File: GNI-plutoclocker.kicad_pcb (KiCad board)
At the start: 2 copper layers, 49 x 47 mm, 67 parts, among them J1 PLUTO_RF_IN, J2 PLUTO_5V, J3 PLUTO_40MHZ_IN, J4 10MHZ_IN, J5 LNB_OUT, J6 10MHZ_OUT, J7 I2C_PROG, J8 18V_ENA, U1 MIC5504-3.3YM5, U2 MIC5504-1.8YM5, U3 TPS61085, U4 CDCE913

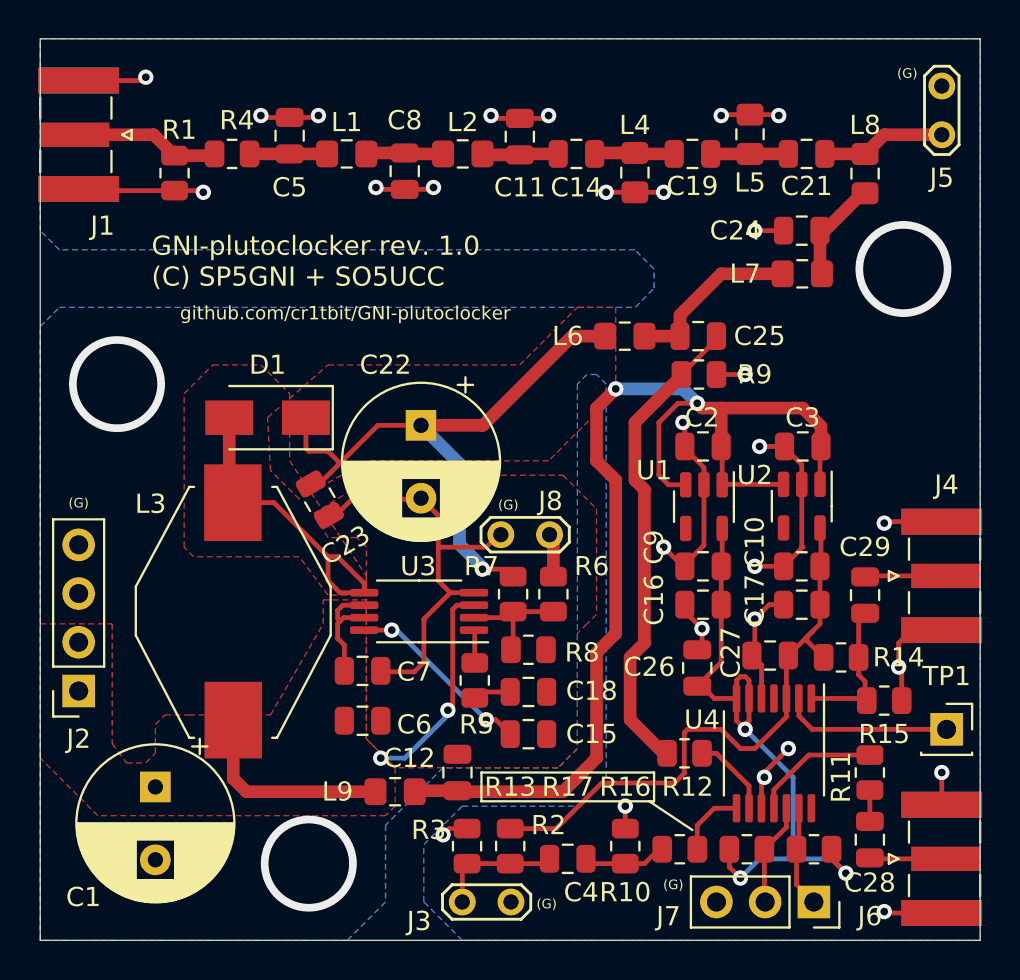
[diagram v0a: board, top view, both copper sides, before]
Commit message: next revision candidate - adding some solderbridge multiplexing options
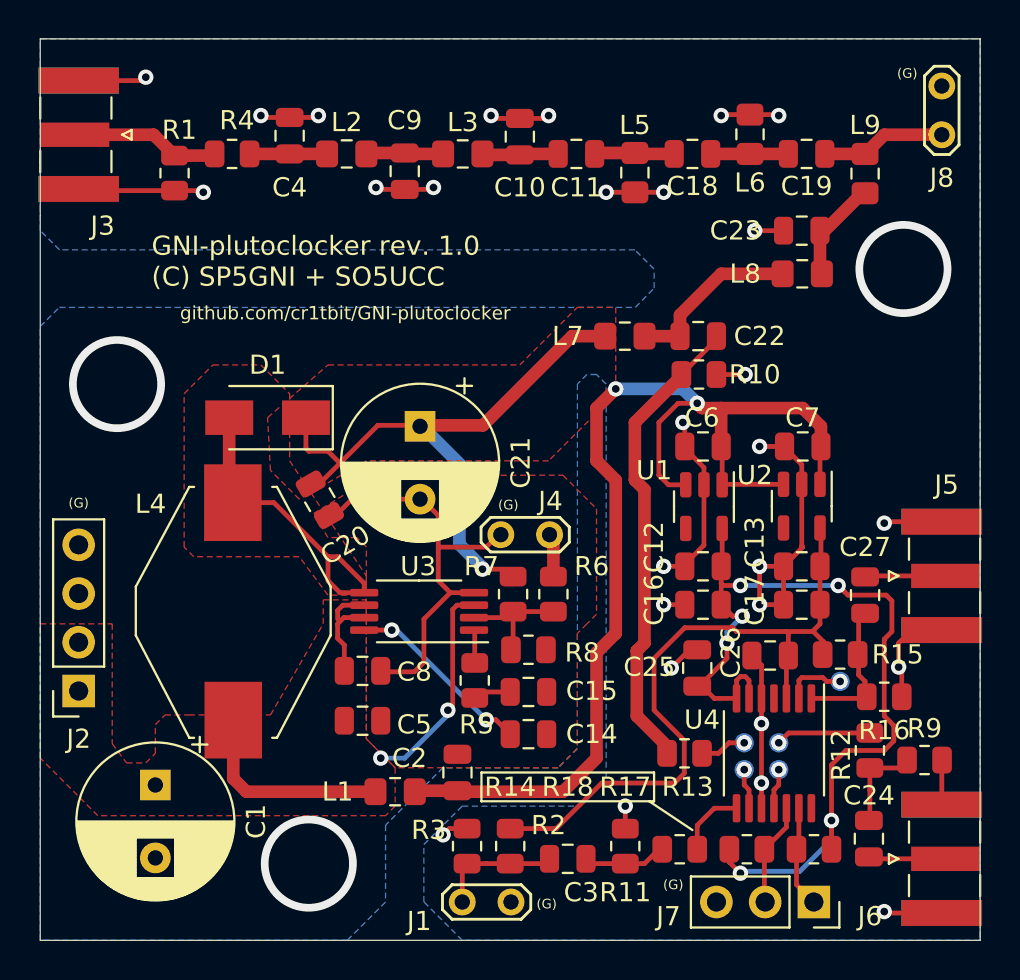
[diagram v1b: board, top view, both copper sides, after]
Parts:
- removed the C22 at (100.8, 70.2)
- added C21: 22u/25v, Capacitor_THT:CP_Radial_D8.0mm_P3.80mm, F.Cu at (100.8, 70.2)
- added R9: 100, Resistor_SMD:R_0805_2012Metric, F.Cu at (127.1, 87.6)
- added TP1: TestPoint_Small, TestPoint:TestPoint_Pad_D1.0mm, B.Cu at (119.5, 86.7)
- added TP2: TestPoint_Small, TestPoint:TestPoint_Pad_D1.0mm, B.Cu at (117.7, 86.7)
- added TP3: TestPoint_Small, TestPoint:TestPoint_Pad_D1.0mm, B.Cu at (119.5, 88.1)
- added TP4: TestPoint_Small, TestPoint:TestPoint_Pad_D1.0mm, B.Cu at (117.7, 88.1)
- C2: renamed from C12; value 10u -> 100n
- C23: renamed from C24; value 47p -> 68p
- J6: value 10MHZ_OUT -> F_OUT
- L1: renamed from L9; value 4.7uH -> 2.2uH
- L7: renamed from L6; value 4.7uH -> 2.2uH
- L8: renamed from L7; value 120nH -> 100nH
- L9: renamed from L8; value 120nH -> 100nH
- R15: renamed from R14; value 100 -> 1k
- R16: renamed from R15; value 100 -> 1k
- R17: renamed from R16; value 4k7 -> DNP
- R18: renamed from R17; value 4k7 -> DNP
- R2, R3: value 100 -> DNP
- TP5: renamed from TP1; footprint Connector_PinSocket_2.54mm:PinSocket_1x01_P2.54mm_Vertical -> TestPoint:TestPoint_Pad_D1.0mm; moved to B.Cu
- moved TP5 6.09 mm to (122.7, 83.5)
- moved R12 1.15 mm to (124.2, 87.1)
- moved R16 0.20 mm to (125.0, 84.3)
- moved R15 0.16 mm to (122.7, 82.1)
- moved C1 0.10 mm to (87.0, 88.9)
- moved C24 0.07 mm to (124.2, 91.7), turned to 270 degrees
- renumbered C11 to C10, C14 to C11, C9 to C12, C10 to C13, C15 to C14, C18 to C15, C19 to C18, C21 to C19, C23 to C20, C25 to C22, C28 to C24, C26 to C25, C27 to C26, C29 to C27, C4 to C3, C5 to C4, C6 to C5, C2 to C6, C3 to C7, C7 to C8, C8 to C9, J3 to J1, J1 to J3, J8 to J4, J4 to J5, J5 to J8, L1 to L2, L2 to L3, L3 to L4, L4 to L5, L5 to L6, R9 to R10, R10 to R11, R11 to R12, R12 to R13, R13 to R14
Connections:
- C24 pad 1: Net-(C28-Pad1) -> Net-(C24-Pad1)
- C24 pad 2: Net-(C28-Pad2) -> Net-(C24-Pad2)
- J6 pad 1: Net-(C28-Pad1) -> Net-(C24-Pad2)
- R12 pad 1: Net-(R11-Pad1) -> Net-(R12-Pad1)
- R12 pad 2: Net-(C28-Pad2) -> Net-(C24-Pad1)
- R13 pad 1: Net-(R12-Pad1) -> Net-(R13-Pad1)
- U4 pad 11: Net-(R11-Pad1) -> Net-(TP3-Pad1)
- U4 pad 9: Net-(R12-Pad1) -> Net-(TP4-Pad1)
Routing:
- net +3V3: track 34.5 -> 48.1 mm, vias 3 -> 6
- net Net-(R11-Pad1): track 6.71 -> 0.00 mm
- net Net-(TP5-Pad1): track 8.90 -> 3.23 mm, vias 0 -> 1
- net +1V8: track 31.4 -> 36.8 mm
- net Net-(C24-Pad1): track 0.00 -> 4.90 mm
- net Net-(C28-Pad1): track 3.97 -> 0.00 mm
- net Net-(C24-Pad2): track 0.00 -> 3.97 mm
- net GND: track 99.0 -> 101.9 mm
- net Net-(R13-Pad1): track 0.00 -> 2.43 mm, vias 0 -> 1
- net Net-(TP4-Pad1): track 0.00 -> 2.12 mm, vias 0 -> 1
- net Net-(TP3-Pad1): track 0.00 -> 2.12 mm, vias 0 -> 1
- net Net-(C28-Pad2): track 1.64 -> 0.00 mm
- net Net-(R12-Pad1): track 4.32 -> 4.96 mm, vias 0 -> 1
- added copper zone on F.Cu, net Net-(C22-Pad1)
- removed copper zone on F.Cu, net Net-(C20-Pad1)
